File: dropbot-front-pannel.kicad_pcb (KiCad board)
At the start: 2 copper layers, 108.3 x 68.8 mm, 15 parts, among them P1 SFM-105-02-L-D-A, P10 CONN_01X02, P11 USB_A, P12 USB_B, P2 SFM-125-02-L-D-A, P3 TFM-125-02-L-DH, P4 SFM-125-02-L-D-A, P5 TFM-125-02-L-DH, P6 SFM-125-02-L-D-A, P7 TFM-125-02-L-DH, P9 CONN_01X03, Q1 IRF9388TRPBF, U2 D24V22F3

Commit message: Add switching/control board outlines
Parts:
- moved JP1 89.8 mm to (-3.81, -5.23)
- moved JP2 89.8 mm to (-8.40, -5.05)
- moved P1 89.8 mm to (27.5, -52.1)
- moved P10 89.8 mm to (-39.7, -4.05)
- moved P11 89.8 mm to (-44.0, -51.1)
- moved P12 89.8 mm to (-43.6, -41.9)
- moved P2 89.8 mm to (19.9, -43.2)
- moved P3 89.8 mm to (36.7, -68.2)
- moved P4 89.8 mm to (19.9, -26.6)
- moved P5 89.8 mm to (0.00, -68.2)
- moved P6 89.8 mm to (19.9, -10.1)
- moved P7 89.8 mm to (-36.7, -68.2)
- moved P9 89.8 mm to (-3.75, -30.6)
- moved Q1 89.8 mm to (-30.2, -8.70)
- moved U2 89.8 mm to (-35.5, -16.1)
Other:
- outline, holes or cut-outs redrawn
- board text added: "Control board"
- board text added: "Switching board 0-39"
- board text added: "Switching board 40-79"
- board text added: "Switching board 80-119"
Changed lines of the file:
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@@
-(kicad_pcb (version 4) (host pcbnew 4.0.1-stable)
+(kicad_pcb (version 4) (host pcbnew 4.0.5)
   (general
     (links 184)
     (no_connects 179)
-    (area -54.215101 20.924999 54.215101 89.825001)
+    (area -56.626101 18.723 56.626101 89.825001)
     (thickness 1.6)
-    (drawings 9)
+    (drawings 29)
     (tracks 0)
     (zones 0)
@@
   )
   (layers
-    (0 F.Cu signal)
+    (0 F.Cu signal hide)
     (31 B.Cu signal)
     (32 B.Adhes user)
@@
   )
   (module Pin_Headers:Pin_Header_Straight_1x03 (layer F.Cu)
-    (at -3.75 59.2)
+    (at -3.75 -30.55)
     (descr "Through hole pin header")
     (tags "pin header")
@@
   )
   (module WheelerLab:TFM-120-02-X-DH (layer F.Cu)
-    (at -36.7284 21.5138)
+    (at -36.7284 -68.2362)
     (descr "0.050\" DOUBLE HORIZONTAL TERMINAL STRIP.")
     (tags "0.050\" DOUBLE HORIZONTAL TERMINAL STRIP.")
@@
   )
   (module WheelerLab:TFM-120-02-X-DH (layer F.Cu)
-    (at 36.7284 21.5138)
+    (at 36.7284 -68.2362)
     (descr "0.050\" DOUBLE HORIZONTAL TERMINAL STRIP.")
     (tags "0.050\" DOUBLE HORIZONTAL TERMINAL STRIP.")
@@
   )
   (module WheelerLab:SFM-105-02-XXX-D-A (layer F.Cu)
-    (at 27.5 37.6)
+    (at 27.5 -52.15)
     (descr "0.05\"X0.05\" SOCKET STRIP DOUBLE ROW ASSEMBLY.")
     (tags "0.05\"X0.05\" SOCKET STRIP DOUBLE ROW ASSEMBLY.")
@@
   )
   (module WheelerLab:SFM-125-02-XXX-D-A (layer F.Cu)
-    (at 19.9 46.5)
+    (at 19.9 -43.25)
     (descr "0.05\"X0.05\" SOCKET STRIP DOUBLE ROW ASSEMBLY.")
     (tags "0.05\"X0.05\" SOCKET STRIP DOUBLE ROW ASSEMBLY.")
@@
   )
   (module WheelerLab:SFM-125-02-XXX-D-A (layer F.Cu)
-    (at 19.9 63.1)
+    (at 19.9 -26.65)
     (descr "0.05\"X0.05\" SOCKET STRIP DOUBLE ROW ASSEMBLY.")
     (tags "0.05\"X0.05\" SOCKET STRIP DOUBLE ROW ASSEMBLY.")
@@
   )
   (module WheelerLab:SFM-125-02-XXX-D-A (layer F.Cu)
-    (at 19.9 79.7)
+    (at 19.9 -10.05)
     (descr "0.05\"X0.05\" SOCKET STRIP DOUBLE ROW ASSEMBLY.")
     (tags "0.05\"X0.05\" SOCKET STRIP DOUBLE ROW ASSEMBLY.")
@@
   )
   (module Connect:bornier2 (layer F.Cu)
-    (at -39.7 85.7 90)
+    (at -39.7 -4.05 90)
     (descr "Bornier d'alimentation 2 pins")
     (tags DEV)
@@
   )
   (module Power_Integrations:SO-8 (layer F.Cu)
-    (at -30.2 81.05)
+    (at -30.2 -8.7)
     (descr "SO-8 Surface Mount Small Outline 150mil 8pin Package")
     (tags "Power Integrations D Package")
@@
   )
   (module WheelerLab:D24V22F (layer F.Cu)
-    (at -35.5 73.65 90)
+    (at -35.5 -16.1 90)
     (fp_text reference U2 (at 9.1 1.1 90) (layer F.SilkS)
       (effects (font (size 1 1) (thickness 0.15)))
@@
   )
   (module Resistors_SMD:R_0805 (layer F.Cu)
-    (at -3.8055 84.5235 90)
+    (at -3.8055 -5.2265 90)
     (descr "Resistor SMD 0805, reflow soldering, Vishay (see dcrcw.pdf)")
     (tags "resistor 0805")
@@
   )
   (module Resistors_SMD:R_0805 (layer F.Cu)
-    (at -8.4 84.7 90)
+    (at -8.4 -5.05 90)
     (descr "Resistor SMD 0805, reflow soldering, Vishay (see dcrcw.pdf)")
     (tags "resistor 0805")
@@
   )
   (module WheelerLab:TFM-125-02-X-DH (layer F.Cu)
-    (at 0 21.5138)
+    (at 0 -68.2362)
     (descr "0.050\" DOUBLE HORIZONTAL TERMINAL STRIP.")
     (tags "0.050\" DOUBLE HORIZONTAL TERMINAL STRIP.")
@@
   )
   (module WheelerLab:1734517-1 (layer B.Cu)
-    (at -43.6 47.9)
+    (at -43.6 -41.85)
     (descr "USB B female connector, straight, rugged")
     (tags "USB_B_MUSB_Straight female connector straight rugged MUSB D511")
@@
   )
   (module WheelerLab:UE27AE54100 (layer F.Cu)
-    (at -44 38.6)
+    (at -44 -51.15)
     (descr "USB A connector")
     (tags "USB USB_A")
@@
     )
   )
-  (gr_line (start 54.1401 81.75) (end 49.1401 81.75) (angle 90) (layer Edge.Cuts) (width 0.15))
-  (gr_line (start 49.1401 81.75) (end 49.1401 89.75) (angle 90) (layer Edge.Cuts) (width 0.15))
-  (gr_line (start -49.1401 81.75) (end -49.1401 89.75) (angle 90) (layer Edge.Cuts) (width 0.15))
-  (gr_line (start -54.1401 81.75) (end -49.1401 81.75) (angle 90) (layer Edge.Cuts) (width 0.15))
-  (gr_text "DropBot front pannel v0.2" (at 37.5 35.55) (layer B.SilkS)
+  (gr_text "Switching board 0-39" (at -33.665928 -8.6995) (layer F.SilkS)
+    (effects (font (size 1.5 1.5) (thickness 0.3)) (justify left))
+  )
+  (gr_text "Switching board 40-79" (at -33.665928 -22.225) (layer F.SilkS)
+    (effects (font (size 1.5 1.5) (thickness 0.3)) (justify left))
+  )
+  (gr_text "Switching board 80-119" (at -33.665928 -35.687) (layer F.SilkS)
+    (effects (font (size 1.5 1.5) (thickness 0.3)) (justify left))
+  )
+  (gr_text "Control board" (at -25.8445 -49.4665) (layer F.SilkS)
+    (effects (font (size 1.5 1.5) (thickness 0.3)))
+  )
+  (gr_line (start -34.163 -34.439) (end -34.163 -32.839) (layer F.SilkS) (width 0.2))
+  (gr_line (start -34.163 -19.239) (end -34.163 -20.839) (layer F.SilkS) (width 0.2))
+  (gr_line (start -34.163 -5.639) (end -34.163 -7.239) (layer F.SilkS) (width 0.2))
+  (gr_line (start 49.7384 -5.639) (end 49.7384 -7.239) (layer F.SilkS) (width 0.2))
+  (gr_line (start 49.7384 -19.239) (end 49.7384 -20.839) (layer F.SilkS) (width 0.2))
+  (gr_line (start 49.7384 -32.839) (end 49.7384 -34.439) (layer F.SilkS) (width 0.2))
+  (gr_line (start -34.1616 -34.439) (end 49.7384 -34.439) (layer F.SilkS) (width 0.2))
+  (gr_line (start -34.1616 -5.639) (end 49.7384 -5.639) (layer F.SilkS) (width 0.2))
+  (gr_line (start -34.1616 -7.239) (end 49.7384 -7.239) (layer F.SilkS) (width 0.2))
+  (gr_line (start -34.1616 -19.239) (end 49.7384 -19.239) (layer F.SilkS) (width 0.2))
+  (gr_line (start -34.1616 -20.839) (end 49.7384 -20.839) (layer F.SilkS) (width 0.2))
+  (gr_line (start -34.1616 -32.839) (end 49.7384 -32.839) (layer F.SilkS) (width 0.2))
+  (gr_line (start 49.7384 -46.439) (end 49.7384 -48.039) (layer F.SilkS) (width 0.2))
+  (gr_line (start -34.1616 -46.439) (end 49.7384 -46.439) (layer F.SilkS) (width 0.2))
+  (gr_line (start -34.1616 -46.439) (end -34.1616 -48.039) (layer F.SilkS) (width 0.2))
+  (gr_line (start 49.7384 -48.039) (end -34.1616 -48.039) (layer F.SilkS) (width 0.2))
+  (gr_line (start 54.1401 -9.239) (end 49.7384 -9.239) (angle 90) (layer Edge.Cuts) (width 0.15))
+  (gr_line (start 49.7384 -9.239) (end 49.7384 0) (angle 90) (layer Edge.Cuts) (width 0.15))
+  (gr_line (start -49.7384 -9.239) (end -49.7384 0) (angle 90) (layer Edge.Cuts) (width 0.15))
+  (gr_line (start -54.1401 -9.239) (end -49.7384 -9.239) (angle 90) (layer Edge.Cuts) (width 0.15))
+  (gr_text "DropBot front pannel v0.2" (at 37.5 -54.2) (layer B.SilkS)
     (effects (font (size 1.5 1.5) (thickness 0.3)) (justify mirror))
   )
-  (gr_line (start 54.1401 81.75) (end 54.1401 21) (angle 90) (layer Edge.Cuts) (width 0.15))
-  (gr_line (start -54.1401 81.75) (end -54.1401 21) (angle 90) (layer Edge.Cuts) (width 0.15))
-  (gr_line (start 49.1401 89.75) (end -49.1401 89.75) (angle 90) (layer Edge.Cuts) (width 0.15))
-  (gr_line (start -54.1401 21) (end 54.1401 21) (angle 90) (layer Edge.Cuts) (width 0.15))
+  (gr_line (start 54.1401 -9.239) (end 54.1401 -68.75) (angle 90) (layer Edge.Cuts) (width 0.15))
+  (gr_line (start -54.1401 -9.239) (end -54.1401 -68.75) (angle 90) (layer Edge.Cuts) (width 0.15))
+  (gr_line (start 49.7384 0) (end -49.7384 0) (angle 90) (layer Edge.Cuts) (width 0.15))
+  (gr_line (start -54.1401 -68.75) (end 54.1401 -68.75) (angle 90) (layer Edge.Cuts) (width 0.15))
   (zone (net 2) (net_name GND) (layer F.Cu) (hatch edge 0.508)
     (connect_pads (clearance 0.6))
@@
     (polygon
       (pts
-        (xy -42 87) (xy -42 21) (xy 42 21) (xy 42 87)
+        (xy -42 -2.75) (xy -42 -68.75) (xy 42 -68.75) (xy 42 -2.75)
       )
     )

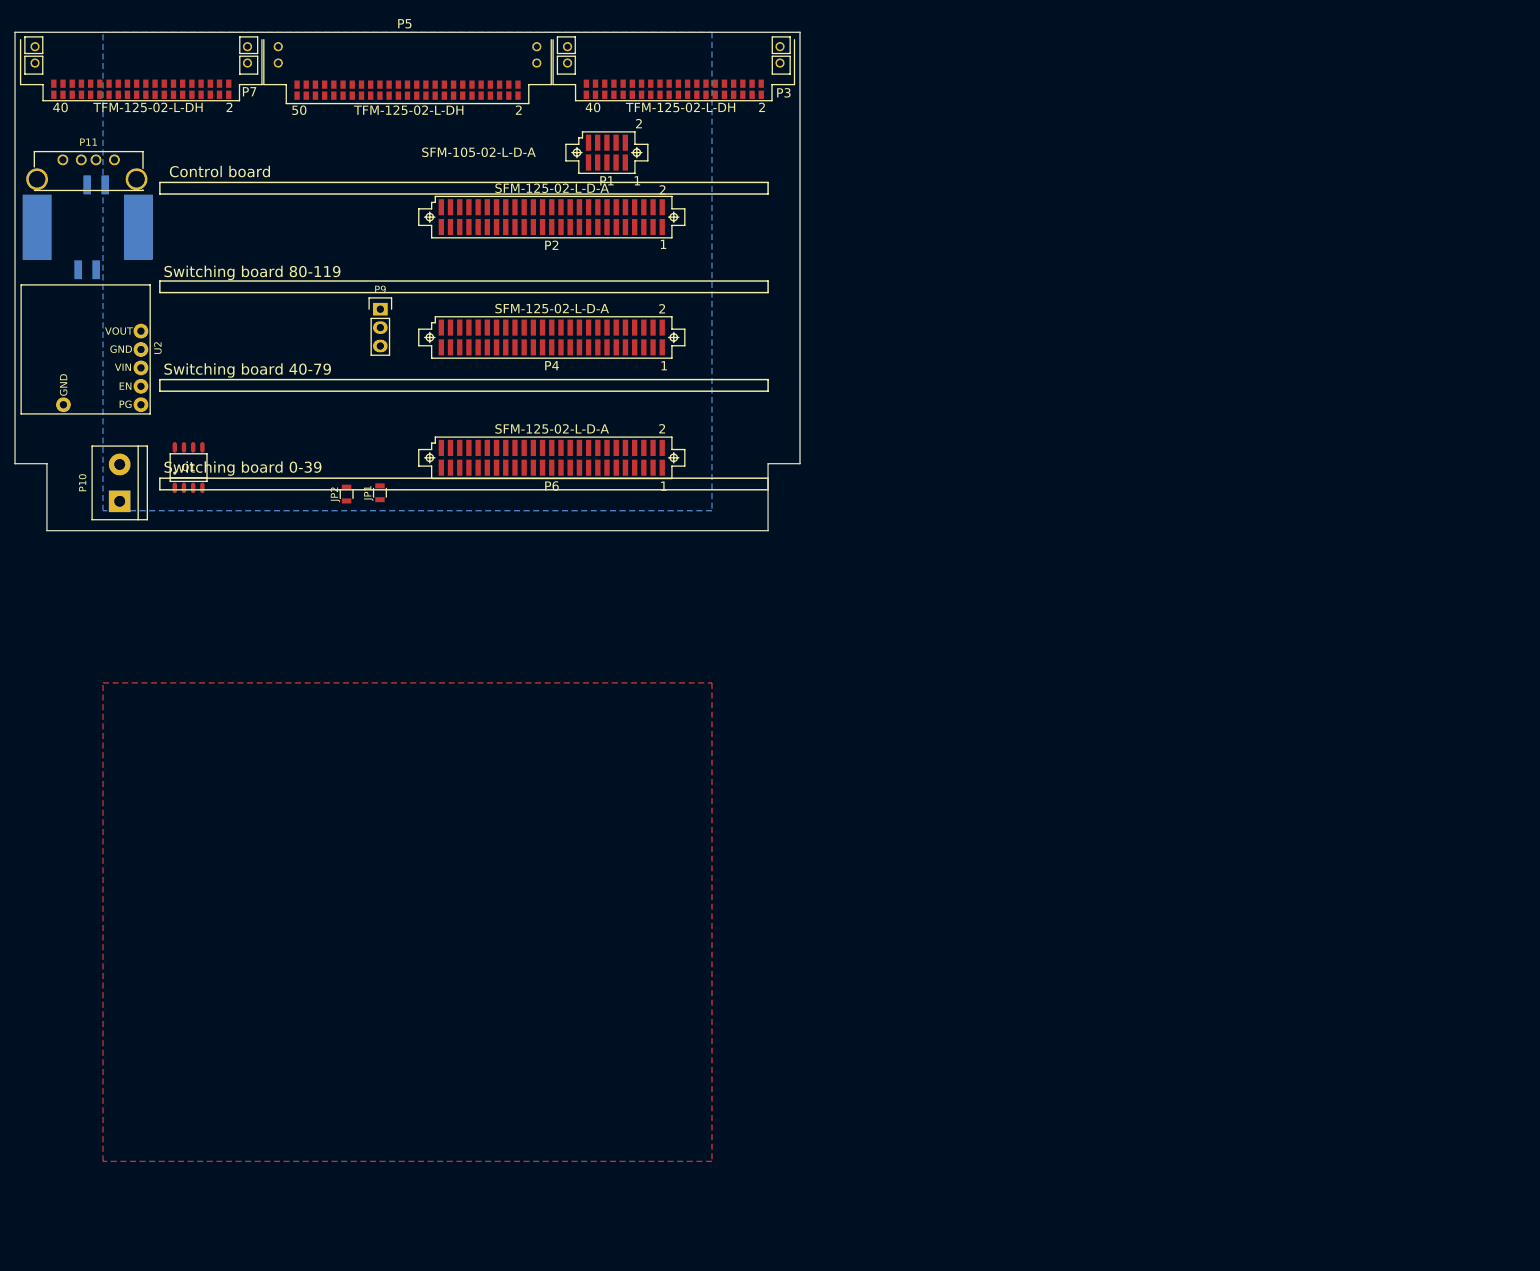
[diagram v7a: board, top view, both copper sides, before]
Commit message: [WIP] Add EMI suppression, ESD protection
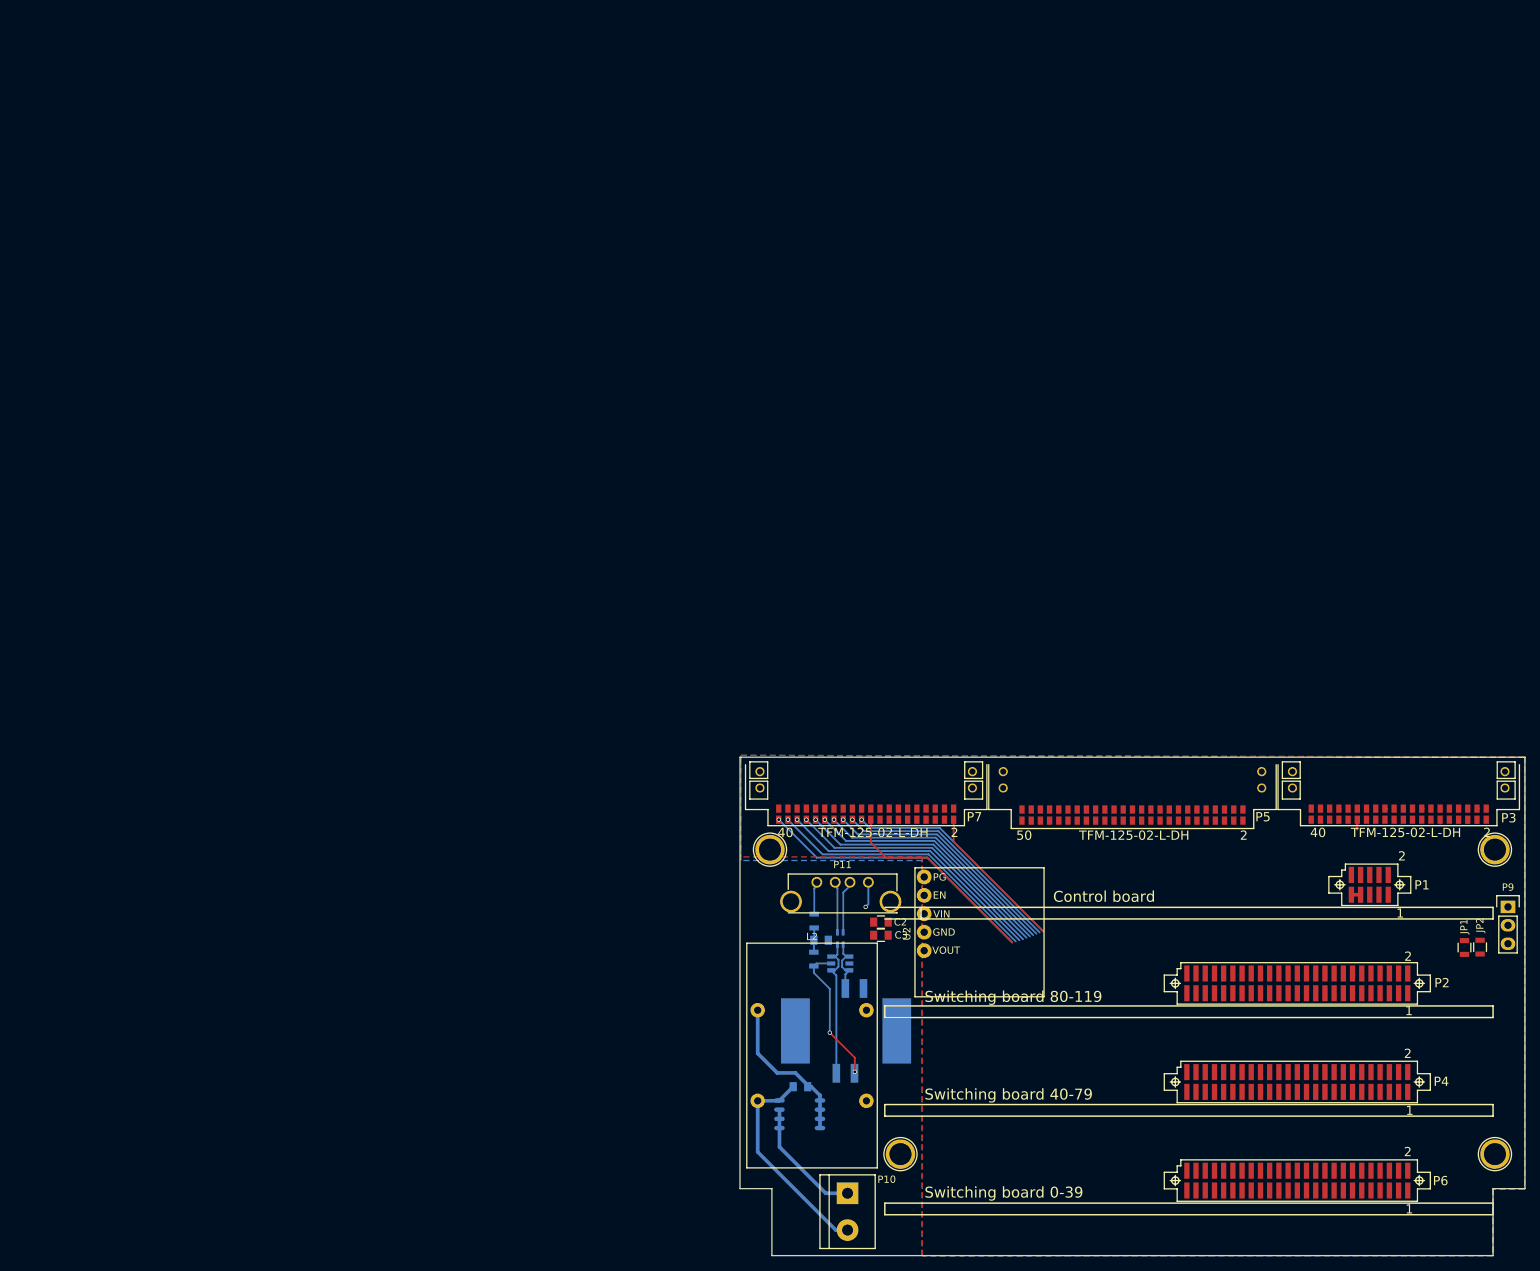
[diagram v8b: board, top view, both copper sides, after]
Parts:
- added C1: 0.1uF, Capacitors_SMD:C_0805, B.Cu at (54.2, 76.7)
- added C2: 0.1uF, Capacitors_SMD:C_0805, F.Cu at (65.3, 54.0)
- added C3: 0.1uF, Capacitors_SMD:C_0805, F.Cu at (65.3, 55.8)
- added C4: 0.1uF, Capacitors_SMD:C_0805, B.Cu at (57.0, 56.5)
- added D1: WE-TVS_824015, WheelerLab:wurth-WE-TVS_SOT23-6L, B.Cu at (59.7, 59.7)
- added FB1: 600 Ohm@100MHz, Resistors_SMD:R_0805, B.Cu at (56.0, 59.1)
- added FB2: 600 Ohm@100MHz, Resistors_SMD:R_0805, B.Cu at (56.1, 53.9)
- added L1: 90 Ohm@100MHz, WheelerLab:wurth-WE-CNSW_0805, B.Cu at (59.7, 56.2)
- added L2: 1.8mH, WheelerLab:RN242-X-02-XXX, F.Cu at (55.8, 72.4)
- added P13: CONN_01X01, Connect:1pin, F.Cu at (150.0, 44.0)
- added P14: CONN_01X01, Connect:1pin, F.Cu at (150.0, 86.0)
- added P15: CONN_01X01, Connect:1pin, F.Cu at (68.0, 86.0)
- added P8: CONN_01X01, Connect:1pin, F.Cu at (50.0, 44.0)
- Q1: moved to B.Cu
- moved P9 176.1 mm to (151.8, 51.9)
- moved JP2 168.4 mm to (147.9, 57.5)
- moved JP1 162.2 mm to (145.8, 57.5)
- moved P12 152.4 mm to (61.0, 69.0)
- moved P2 147.5 mm to (122.7, 62.4)
- moved P1 145.9 mm to (132.7, 48.8)
- moved P4 145.3 mm to (122.7, 76.0)
- moved P11 144.0 mm to (60.0, 48.5)
- moved P6 143.2 mm to (122.7, 89.6)
- moved P3 141.4 mm to (136.7, 31.8)
- moved P5 141.4 mm to (100.0, 31.8)
- moved P7 141.4 mm to (63.3, 31.8)
- moved P10 138.5 mm to (60.7, 91.4), turned to 270 degrees
- moved Q1 122.7 mm to (54.1, 80.5), turned to 90 degrees
- moved U2 122.7 mm to (70.0, 46.5), turned to 270 degrees
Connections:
- net V_IN renamed +12V_SUPPLY
- P10 pad 2: GND -> CHASIS_GND
- P11 pad 2: Net-(P11-Pad2) -> Net-(L1-Pad3)
- P11 pad 3: Net-(P11-Pad3) -> Net-(L1-Pad2)
- P12 pad 2: Net-(P11-Pad2) -> Net-(D1-Pad4)
- P12 pad 3: Net-(P11-Pad3) -> Net-(D1-Pad1)
- P2 pad 1: HVOUT0 -> SDA
- P2 pad 10: HVOUT9 -> HVGND
- P2 pad 11: HVOUT10 -> HVOUT39
- P2 pad 12: HVOUT11 -> HVOUT38
- P2 pad 13: HVOUT12 -> HVOUT37
- P2 pad 14: HVOUT13 -> HVOUT36
- P2 pad 15: HVOUT14 -> HVOUT35
- P2 pad 16: HVOUT15 -> HVOUT34
- P2 pad 17: HVOUT16 -> HVOUT33
- P2 pad 18: HVOUT17 -> HVOUT32
- P2 pad 19: HVOUT18 -> HVOUT31
- P2 pad 2: HVOUT1 -> +3.3V
- P2 pad 20: HVOUT19 -> HVOUT30
- P2 pad 21: HVOUT20 -> HVOUT29
- P2 pad 22: HVOUT21 -> HVOUT28
- P2 pad 23: HVOUT22 -> HVOUT27
- P2 pad 24: HVOUT23 -> HVOUT26
- P2 pad 25: HVOUT24 -> HVOUT25
- P2 pad 26: HVOUT25 -> HVOUT24
- P2 pad 27: HVOUT26 -> HVOUT23
- P2 pad 28: HVOUT27 -> HVOUT22
- P2 pad 29: HVOUT28 -> HVOUT21
- P2 pad 3: HVOUT2 -> GND
- P2 pad 30: HVOUT29 -> HVOUT20
- P2 pad 31: HVOUT30 -> HVOUT19
- P2 pad 32: HVOUT31 -> HVOUT18
- P2 pad 33: HVOUT32 -> HVOUT17
- P2 pad 34: HVOUT33 -> HVOUT16
- P2 pad 35: HVOUT34 -> HVOUT15
- P2 pad 36: HVOUT35 -> HVOUT14
- P2 pad 37: HVOUT36 -> HVOUT13
- P2 pad 38: HVOUT37 -> HVOUT12
- P2 pad 39: HVOUT38 -> HVOUT11
- P2 pad 4: HVOUT3 -> +3.3V
- P2 pad 40: HVOUT39 -> HVOUT10
- P2 pad 41: HVAC -> HVOUT9
- P2 pad 42: HVGND -> HVOUT8
- P2 pad 43: GND -> HVOUT7
- P2 pad 44: RST1 -> HVOUT6
- P2 pad 45: GND -> HVOUT5
- P2 pad 46: SCL -> HVOUT4
- P2 pad 47: GND -> HVOUT3
- P2 pad 48: +3.3V -> HVOUT2
- P2 pad 49: SDA -> HVOUT1
- P2 pad 5: HVOUT4 -> GND
- P2 pad 50: +3.3V -> HVOUT0
- P2 pad 6: HVOUT5 -> SCL
- P2 pad 7: HVOUT6 -> GND
- P2 pad 8: HVOUT7 -> RST1
- P2 pad 9: HVOUT8 -> HVAC
- P4 pad 1: HVOUT40 -> SDA
- P4 pad 10: HVOUT49 -> HVGND
- P4 pad 11: HVOUT50 -> HVOUT79
- P4 pad 12: HVOUT51 -> HVOUT78
- P4 pad 13: HVOUT52 -> HVOUT77
- P4 pad 14: HVOUT53 -> HVOUT76
- P4 pad 15: HVOUT54 -> HVOUT75
- P4 pad 16: HVOUT55 -> HVOUT74
- P4 pad 17: HVOUT56 -> HVOUT73
- P4 pad 18: HVOUT57 -> HVOUT72
- P4 pad 19: HVOUT58 -> HVOUT71
- P4 pad 2: HVOUT41 -> +3.3V
- P4 pad 20: HVOUT59 -> HVOUT70
- P4 pad 21: HVOUT60 -> HVOUT69
- P4 pad 22: HVOUT61 -> HVOUT68
- P4 pad 23: HVOUT62 -> HVOUT67
- P4 pad 24: HVOUT63 -> HVOUT66
- P4 pad 25: HVOUT64 -> HVOUT65
- P4 pad 26: HVOUT65 -> HVOUT64
- P4 pad 27: HVOUT66 -> HVOUT63
- P4 pad 28: HVOUT67 -> HVOUT62
- P4 pad 29: HVOUT68 -> HVOUT61
- P4 pad 3: HVOUT42 -> GND
- P4 pad 30: HVOUT69 -> HVOUT60
- P4 pad 31: HVOUT70 -> HVOUT59
- P4 pad 32: HVOUT71 -> HVOUT58
- P4 pad 33: HVOUT72 -> HVOUT57
- P4 pad 34: HVOUT73 -> HVOUT56
- P4 pad 35: HVOUT74 -> HVOUT55
- P4 pad 36: HVOUT75 -> HVOUT54
- P4 pad 37: HVOUT76 -> HVOUT53
- P4 pad 38: HVOUT77 -> HVOUT52
- P4 pad 39: HVOUT78 -> HVOUT51
- P4 pad 4: HVOUT43 -> +3.3V
- P4 pad 40: HVOUT79 -> HVOUT50
- P4 pad 41: HVAC -> HVOUT49
- P4 pad 42: HVGND -> HVOUT48
- P4 pad 43: GND -> HVOUT47
- P4 pad 44: RST2 -> HVOUT46
- P4 pad 45: GND -> HVOUT45
- P4 pad 46: SCL -> HVOUT44
- P4 pad 47: GND -> HVOUT43
- P4 pad 48: +3.3V -> HVOUT42
- P4 pad 49: SDA -> HVOUT41
- P4 pad 5: HVOUT44 -> GND
- P4 pad 50: +3.3V -> HVOUT40
- P4 pad 6: HVOUT45 -> SCL
- P4 pad 7: HVOUT46 -> GND
- P4 pad 8: HVOUT47 -> RST2
- P4 pad 9: HVOUT48 -> HVAC
- P6 pad 1: HVOUT80 -> SDA
- P6 pad 10: HVOUT89 -> HVGND
- P6 pad 11: HVOUT90 -> HVOUT119
- P6 pad 12: HVOUT91 -> HVOUT118
- P6 pad 13: HVOUT92 -> HVOUT117
- P6 pad 14: HVOUT93 -> HVOUT116
- P6 pad 15: HVOUT94 -> HVOUT115
- P6 pad 16: HVOUT95 -> HVOUT114
- P6 pad 17: HVOUT96 -> HVOUT113
- P6 pad 18: HVOUT97 -> HVOUT112
- P6 pad 19: HVOUT98 -> HVOUT111
- P6 pad 2: HVOUT81 -> +3.3V
- P6 pad 20: HVOUT99 -> HVOUT110
- P6 pad 21: HVOUT100 -> HVOUT109
- P6 pad 22: HVOUT101 -> HVOUT108
- P6 pad 23: HVOUT102 -> HVOUT107
- P6 pad 24: HVOUT103 -> HVOUT106
- P6 pad 25: HVOUT104 -> HVOUT105
- P6 pad 26: HVOUT105 -> HVOUT104
- P6 pad 27: HVOUT106 -> HVOUT103
- P6 pad 28: HVOUT107 -> HVOUT102
- P6 pad 29: HVOUT108 -> HVOUT101
- P6 pad 3: HVOUT82 -> GND
- P6 pad 30: HVOUT109 -> HVOUT100
- P6 pad 31: HVOUT110 -> HVOUT99
- P6 pad 32: HVOUT111 -> HVOUT98
- P6 pad 33: HVOUT112 -> HVOUT97
- P6 pad 34: HVOUT113 -> HVOUT96
- P6 pad 35: HVOUT114 -> HVOUT95
- P6 pad 36: HVOUT115 -> HVOUT94
- P6 pad 37: HVOUT116 -> HVOUT93
- P6 pad 38: HVOUT117 -> HVOUT92
- P6 pad 39: HVOUT118 -> HVOUT91
- P6 pad 4: HVOUT83 -> +3.3V
- P6 pad 40: HVOUT119 -> HVOUT90
- P6 pad 41: HVAC -> HVOUT89
- P6 pad 42: HVGND -> HVOUT88
- P6 pad 43: GND -> HVOUT87
- P6 pad 44: RST3 -> HVOUT86
- P6 pad 45: GND -> HVOUT85
- P6 pad 46: SCL -> HVOUT84
- P6 pad 47: GND -> HVOUT83
- P6 pad 48: +3.3V -> HVOUT82
- P6 pad 49: SDA -> HVOUT81
- P6 pad 5: HVOUT84 -> GND
- P6 pad 50: +3.3V -> HVOUT80
- P6 pad 6: HVOUT85 -> SCL
- P6 pad 7: HVOUT86 -> GND
- P6 pad 8: HVOUT87 -> RST3
- P6 pad 9: HVOUT88 -> HVAC
- Q1 pad 4: GND -> CHASIS_GND
- Q1 pad 5: +12V -> Net-(C1-Pad1)
- Q1 pad 6: +12V -> Net-(C1-Pad1)
- Q1 pad 7: +12V -> Net-(C1-Pad1)
- Q1 pad 8: +12V -> Net-(C1-Pad1)
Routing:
- net HVOUT119: track 0.00 -> 39.2 mm, vias 0 -> 1
- net HVOUT117: track 0.00 -> 38.4 mm, vias 0 -> 1
- net HVOUT115: track 0.00 -> 37.5 mm, vias 0 -> 1
- net HVOUT113: track 0.00 -> 36.8 mm, vias 0 -> 1
- net HVOUT111: track 0.00 -> 35.9 mm, vias 0 -> 1
- net HVOUT109: track 0.00 -> 35.0 mm, vias 0 -> 1
- net HVOUT107: track 0.00 -> 34.1 mm, vias 0 -> 1
- net HVOUT105: track 0.00 -> 33.2 mm, vias 0 -> 1
- net HVOUT103: track 0.00 -> 32.3 mm, vias 0 -> 1
- net HVOUT101: track 0.00 -> 31.4 mm, vias 0 -> 1
- net CHASIS_GND: track 0.00 -> 29.6 mm
- net HVOUT99: track 0.00 -> 28.3 mm
- net Net-(C1-Pad1): track 0.00 -> 21.6 mm
- net Net-(D1-Pad4): track 0.00 -> 20.6 mm
- net HVOUT81: track 0.00 -> 20.6 mm
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- added copper zone on GND, net CHASIS_GND
- added copper zone on GND, net GND
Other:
- copper layers 2 -> 4
- net class PWR added: clearance 0.2, trace_width 0.5, via_dia 0.6, via_drill 0.4
- board text added: "Move -100, -100 to align coordinates to CAD model."
